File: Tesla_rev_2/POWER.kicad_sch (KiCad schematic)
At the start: 23 parts, among them J11 Screw_Terminal_01x03, U8 AP63203WU

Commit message: revision 3
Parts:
- removed C37: 10uF, symbol Device:C_Polarized
- removed C38, C39, C41, C42: 47uF, symbol Device:C_Polarized
- removed C43, C44: 22uF, symbol Device:C_Polarized
- removed JP4: SolderJp_Open, symbol Jumper:SolderJumper_2_Open
- removed L4: 2.2uF, symbol Device:L
- added C26, C27, C28, C29, C30, C31, C32: 10uF, symbol Device:C
- added C34, C35: 22uF, symbol Device:C
- added J8: USB_C_Receptacle_USB2.0_16P, Connector_USB:USB_C_Receptacle_GCT_USB4105-xx-A_16P_TopMnt_Horizontal, symbol Connector:USB_C_Receptacle_USB2.0_16P
- added JP1, JP2: SolderJumper_Open, symbol Jumper:SolderJumper_2_Open
- added R20: 125, symbol Device:R
- added R21: 820, symbol Device:R
- added R24, R25: 5.1K, symbol Device:R
- added TP3, TP8: TestPoint, symbol Connector:TestPoint
- added U6: LD1117STR, Package_TO_SOT_SMD:SOT-223, symbol Tesla_sextant_BT_Library:LD1117STR
- added U8: USBLC6-2P6, Package_TO_SOT_SMD:SOT-666, symbol Power_Protection:USBLC6-2P6
- JP3: value SolderJp_Open -> SolderJumper_Open
- L2: renamed from L5; value 2.2uF -> L; Part_num DFE32CAH2R2MR0L -> (none)
- R22: value 200m -> 1R; Part_num CS12FTFSR200 -> HP05W3F100KT5E; now not fitted
- R23: value 200m -> 1R; Part_num CS12FTFSR200 -> HP05W3F100KT5E
- renumbered C40 to C33, D3 to D4, D4 to D5, J11 to J7, L6 to L3, TP1 to TP4, TP2 to TP5, TP3 to TP6, TP4 to TP7, U8 to U7
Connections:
- net 13.3V is gone; now on net VBUS: TP6.1
- net +3.3V: now also C34.1, C35.1
- net +5V: now also R23.1, C32.1, U8.5 (VBUS)
- net GND: now also C26.2, C27.2, C28.2, C29.2, C30.2, C31.2, C32.2, C34.2, C35.2, J8.A1 (GND), J8.A12 (GND), J8.B1 (GND), J8.B12 (GND), J8.S1 (SHIELD), R21.2, R24.2, R25.2, U8.2 (GND)
- net POW_+15V: now also R22.2, JP1.1 (A); no longer R22.1
- net POW_5V: now also L2.1, C29.1, TP3.1; no longer R23.1
- net VBUS: now also R22.1, C26.1, C30.1, C31.1, JP1.2 (B), JP2.2 (B), U6.3 (IN); no longer L2.2
- net VUSB: now also J8.A4 (VBUS), J8.A9 (VBUS), J8.B4 (VBUS), J8.B9 (VBUS), JP2.1 (A)
- net at R23.2: now also L2.2; no longer L2.1
- new net: J8.B5 (CC2), R24.1
- new net: C27.1, R20.2, R21.1, U6.1 (ADJ), U6.4 (ADJ)
- new net: J8.A5 (CC1), R25.1
- new net +10V: C28.1, R20.1, TP8.1, U6.2 (OUT)
- new net D+: J8.A6 (D+), J8.B6 (D+), U8.3 (I/O2)
- new net D-: J8.A7 (D-), J8.B7 (D-), U8.1 (I/O1)
- new net USB_D+: U8.4 (I/O2)
- new net USB_D-: U8.6 (I/O1)
- no-connect marks 0 -> 2
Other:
- note added: "Typ. +13 to +15V (U_{br} = 16V)"
- note added: "USB C"
- note removed: "Power from USB, optionally disconnect only for data transfer"
- note removed: "Typ. +13 to +15V"
- moved on the sheet: C33, D4, D5, J7, L2, L3, TP4, TP5, TP6, TP7, U7

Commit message: Rev 2.3, schematic and footprint fixes, prepared for layout
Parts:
- removed J7: Screw_Terminal_01x03, symbol Connector:Screw_Terminal_01x03
- removed U6: LD1117STR, Package_TO_SOT_SMD:SOT-223, symbol Tesla_sextant_BT_Library:LD1117STR
- removed U8: USBLC6-2P6, Package_TO_SOT_SMD:SOT-666, symbol Power_Protection:USBLC6-2P6
- added D4, D6: B220, Diode_SMD:D_SMB, symbol Diode:B220
- added D7: SMAJ5.0A, Diode_SMD:D_SMA, symbol Diode:SMAJ5.0A
- added J7: Conn_01x03, Tesla_Library:Conn_Solder_1x03_SMD, symbol Connector_Generic:Conn_01x03
- added JP3: SolderJumper_Open, Jumper:SolderJumper-2_P1.3mm_Open_TrianglePad1.0x1.5mm, symbol Jumper:SolderJumper_2_Open
- added TP11, TP9: TestPoint, TestPoint:TestPoint_Pad_D2.5mm, symbol Connector:TestPoint
- added U5: USBLC6-2SC6, Package_TO_SOT_SMD:SOT-23-6, symbol Power_Protection:USBLC6-2SC6
- added U7: LD1117STR, Package_TO_SOT_SMD:SOT-223, symbol Tesla_sextant_BT_Library:LM317DCYR
- C18: renamed from C30; footprint (none) -> Capacitor_SMD:C_0805_2012Metric; now left out of the parts list
- C19: renamed from C29; footprint (none) -> Capacitor_SMD:C_0805_2012Metric; now not fitted; now left out of the parts list
- C20: renamed from C32; footprint (none) -> Capacitor_SMD:C_0805_2012Metric; now not fitted; now left out of the parts list
- C21: renamed from C33; footprint (none) -> Capacitor_SMD:C_0805_2012Metric
- C22: renamed from C31; footprint (none) -> Capacitor_SMD:C_0805_2012Metric
- C23: renamed from C34; footprint (none) -> Capacitor_SMD:C_0805_2012Metric
- C24: renamed from C35; footprint (none) -> Capacitor_SMD:C_0805_2012Metric
- C25: renamed from C26; footprint (none) -> Capacitor_SMD:C_0805_2012Metric
- C26: renamed from C28; footprint (none) -> Capacitor_SMD:C_0805_2012Metric
- C27: value 10uF -> 100nF; footprint (none) -> Capacitor_SMD:C_0805_2012Metric
- JP1, JP2: footprint (none) -> Jumper:SolderJumper-2_P1.3mm_Open_TrianglePad1.0x1.5mm
- JP4: renamed from JP3; footprint (none) -> Jumper:SolderJumper-2_P1.3mm_Open_TrianglePad1.0x1.5mm
- L1: renamed from L2; value L -> 2.2uH; footprint (none) -> Inductor_SMD:L_12x12mm_H8mm; Part_num (none) -> DR125-2R2-R; now not fitted; now left out of the parts list
- L2: renamed from L3; footprint (none) -> Inductor_SMD:L_12x12mm_H8mm; Part_num LQH44PN2R2MPRL -> DR125-2R2-R
- R21: renamed from R22; Part_num HP05W3F100KT5E -> 25121WF100KT4E; now left out of the parts list
- R22: renamed from R24; footprint (none) -> Capacitor_SMD:C_0805_2012Metric
- R23: renamed from R25; footprint (none) -> Capacitor_SMD:C_0805_2012Metric
- R24: renamed from R23; Part_num HP05W3F100KT5E -> 25121WF100KT4E; now not fitted; now left out of the parts list
- R25: renamed from R20; value 125 -> 120; footprint (none) -> Capacitor_SMD:C_0805_2012Metric
- R26: renamed from R21; footprint (none) -> Capacitor_SMD:C_0805_2012Metric
- TP10: renamed from TP5; footprint (none) -> TestPoint:TestPoint_Pad_D2.5mm; now left out of the parts list
- TP4: renamed from TP3; footprint (none) -> TestPoint:TestPoint_Pad_D2.5mm; now left out of the parts list
- TP5: renamed from TP4; footprint (none) -> TestPoint:TestPoint_Pad_D2.5mm; now left out of the parts list
- TP6: footprint (none) -> TestPoint:TestPoint_Pad_D2.5mm; now left out of the parts list
- TP7: renamed from TP8; footprint (none) -> TestPoint:TestPoint_Pad_D2.5mm; now left out of the parts list
- TP8: renamed from TP7; footprint (none) -> TestPoint:TestPoint_Pad_D2.5mm; now left out of the parts list
- renumbered D4 to D5, D5 to D8, J8 to J6, U7 to U6
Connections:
- net +10V: now also U7.2 (OUT), U7.4 (OUT)
- net +5V: now also JP3.2 (B), U5.5 (VBUS)
- net GND: now also D7.2 (A2), J7.3 (Pin_3), U5.2 (GND); no longer J6.S1 (SHIELD)
- net POW_+15V: now also D4.1 (K), TP11.1
- net POW_5V: now also D6.1 (K), JP3.1 (A)
- net USB_D+: now also U5.4 (I/O2)
- net USB_D-: now also U5.6 (I/O1)
- net VBUS: now also U7.3 (IN)
- net VUSB: now also D7.1 (A1), TP9.1
- net CC2: now reaches J6.B5 (CC2), R22.1
- net BUCK_FF: now reaches C21.1
- net BUCK_FF: now also U6.6 (BST); no longer U6.5 (SW)
- net BUCK_SW: now reaches C21.2, L2.1
- net BUCK_SW: now also U6.5 (SW); no longer U6.6 (BST)
- net 10V_ADJ: now reaches C27.1, R25.2, R26.1
- net 10V_ADJ: now also U7.1 (ADJ)
- net CC1: now reaches J6.A5 (CC1), R23.1
- net D+ renamed USB_C_D+
- net USB_C_D+: now also U5.3 (I/O2)
- net D- renamed USB_C_D-
- net USB_C_D-: now also U5.1 (I/O1)
- new net POW_1: D4.2 (A), J7.1 (Pin_1)
- new net POW_2: D6.2 (A), J7.2 (Pin_2)
- no-connect marks 2 -> 3
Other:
- note added: "1W 200V"
- note added: "BUCK"
- note added: "Typ. +13 to +15V (TVS U_{br} = 16V)"
- note added: "Uout = ~10V Uout = 1.25 * (1 + (R2/R1)) 10 = 1.25 * (1 + (R2/120)) R2 = 840 => 820"
- note added: "Zenner regulated +5V on Radio board"
- note removed: "Typ. +13 to +15V (U_{br} = 16V)"
- note removed: "Zenner diode regulated +5V on Radio board"
- title: Tesla sextant BT -> Tesla sextant BT POWER
- moved on the sheet: C18, C21, C22, C23, C24, C25, C26, D5, D8, L2, R21, R25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

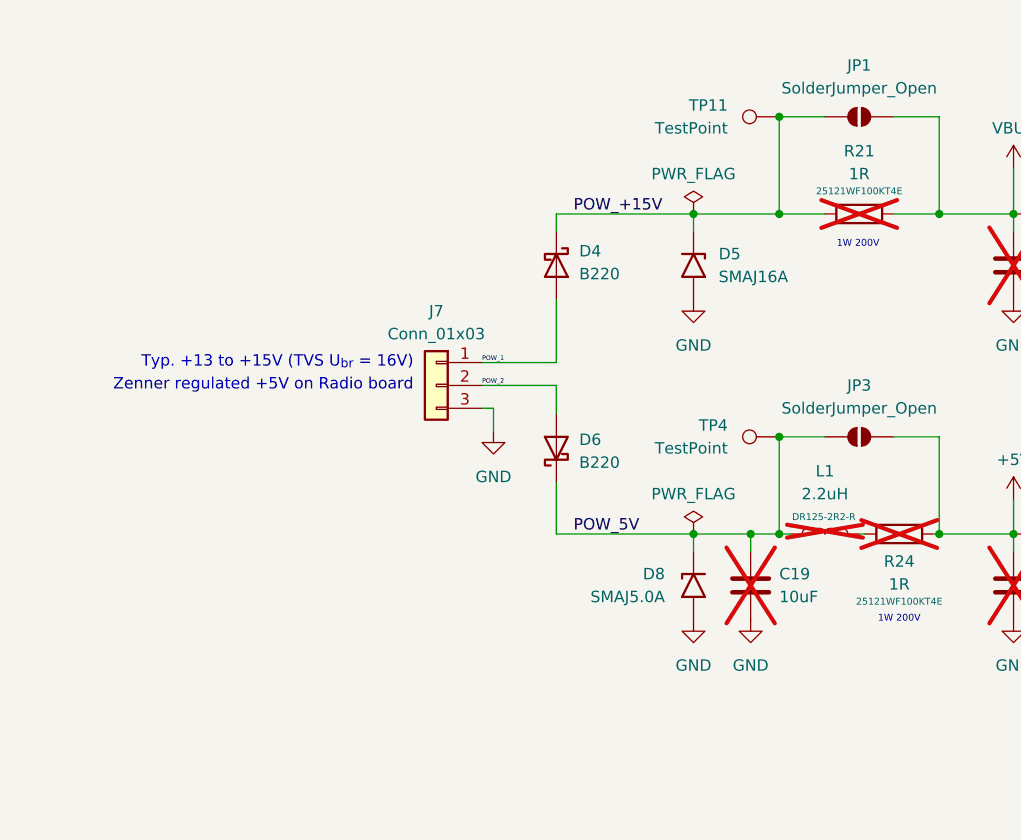
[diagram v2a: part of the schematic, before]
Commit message: added PCB layou
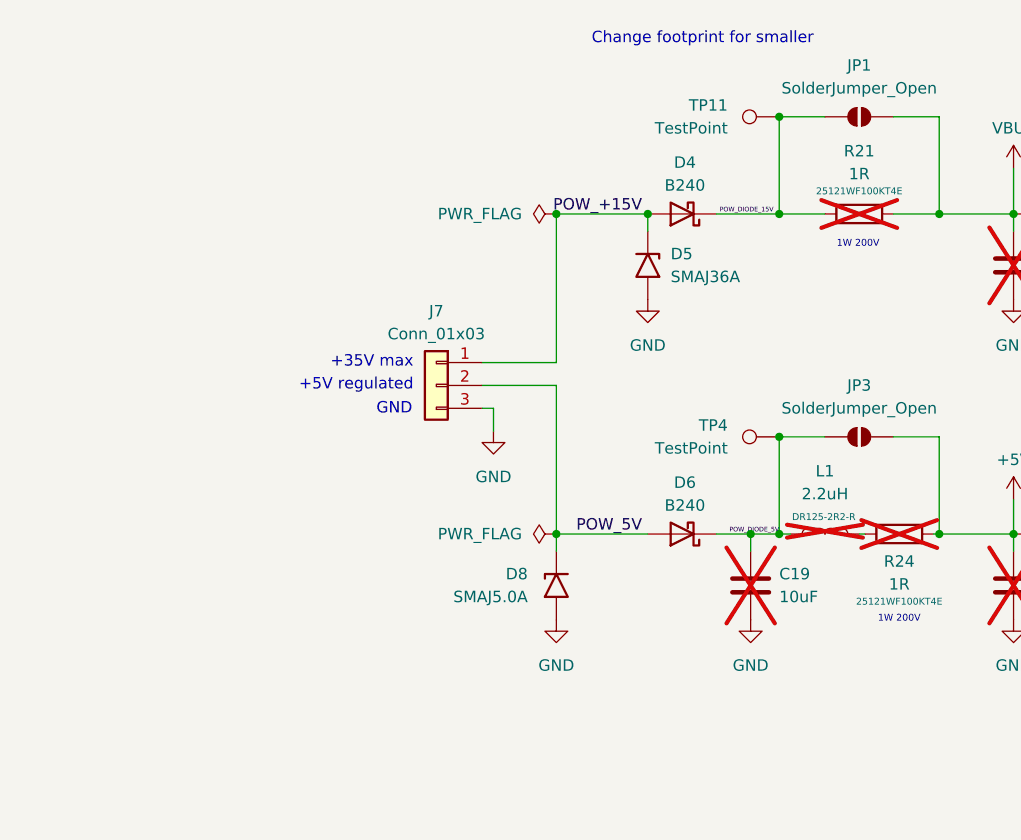
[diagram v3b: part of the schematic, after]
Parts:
- removed D4, D6: B220, Diode_SMD:D_SMB, symbol Diode:B220
- removed D5: SMAJ16A, Diode_SMD:D_SMA, symbol Diode:SMAJ16A
- added D4, D6: B240, Diode_SMD:D_SMB, symbol Diode:B240
- added D5: SMAJ36A, Diode_SMD:D_SMA, symbol Diode:SMAJ36A
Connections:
- net POW_1 is gone; now on net POW_+15V: J7.1 (Pin_1)
- net POW_2 is gone; now on net POW_5V: J7.2 (Pin_2)
- net GND: now also D5.2 (A2)
- net POW_+15V: now also D4.2 (A), D5.1 (A1); no longer JP1.1 (A), R21.2, TP11.1
- net POW_5V: now also D6.2 (A); no longer C19.1, JP3.1 (A), L1.1, TP4.1
- new net POW_DIODE_15V: D4.1 (K), JP1.1 (A), R21.2, TP11.1
- new net POW_DIODE_5V: C19.1, D6.1 (K), JP3.1 (A), L1.1, TP4.1
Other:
- note added: "+35V max"
- note added: "+5V regulated"
- note added: "Change footprint for smaller"
- note added: "GND"
- note removed: "Typ. +13 to +15V (TVS U_{br} = 16V)"
- note removed: "Zenner regulated +5V on Radio board"
- moved on the sheet: D8
